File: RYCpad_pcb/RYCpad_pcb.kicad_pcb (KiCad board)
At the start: 2 copper layers, 77.2 x 117.6 mm, 69 parts, among them J1 USB_C_Receptacle_USB2.0, J2 AVR ISP, K1 KEYSW, K10 KEYSW, K11 KEYSW, K12 KEYSW, K13 KEYSW, K14 KEYSW, K15 KEYSW, K16 KEYSW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

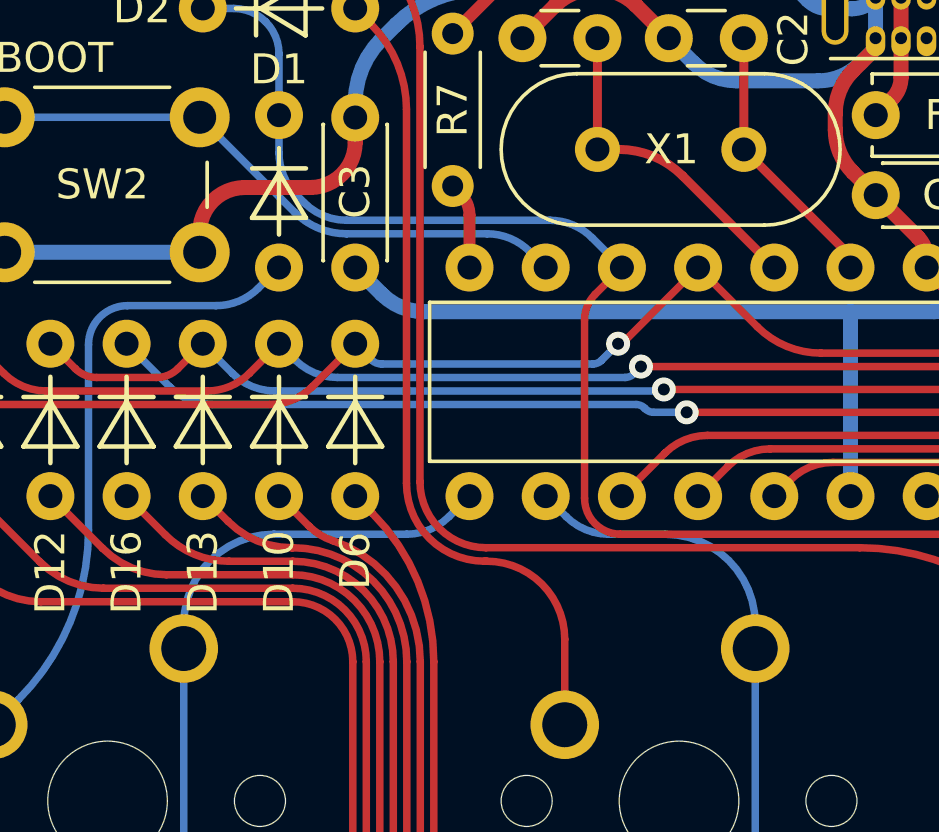
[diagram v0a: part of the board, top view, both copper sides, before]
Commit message: update LED pin
- QMK supports hardware PWM on pin PB1 and PB2 for backlight dimming.
  The hope is that hardware PWM dimming can be exploited for the
  indicator LED, which mitigates any issues related to excessive LED
  brightness.
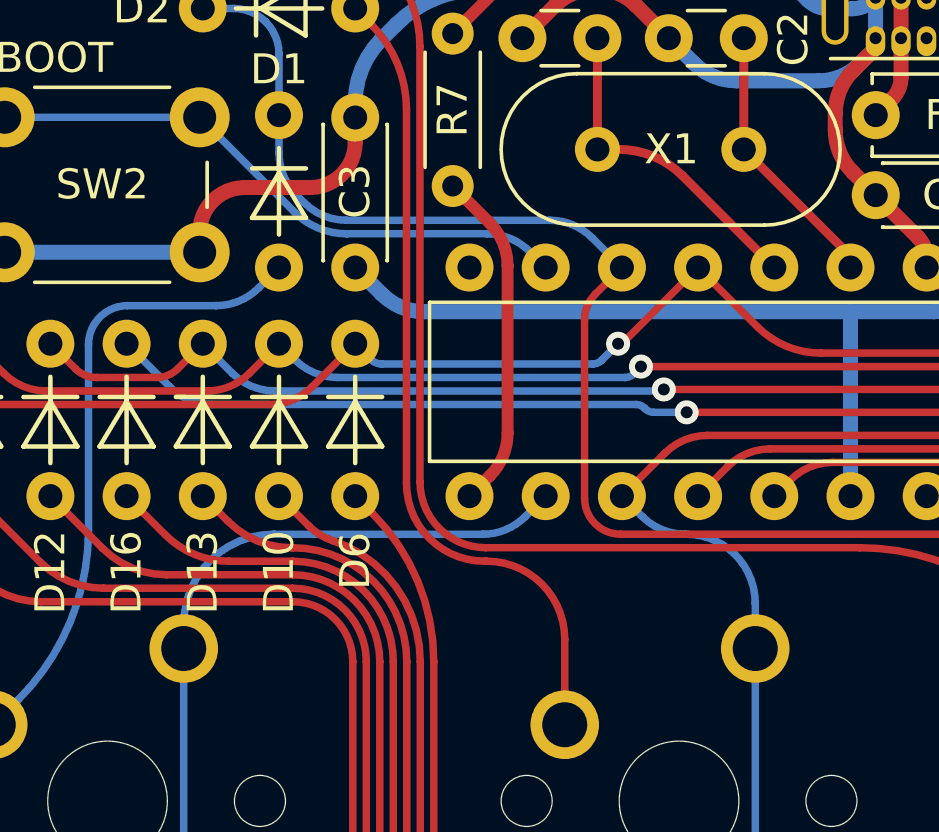
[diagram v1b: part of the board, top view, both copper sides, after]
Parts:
- D20: value LTL-4221N -> LED
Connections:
- J2 pad 4: /MOSI -> /MOSI/col1
- K10 pad 1: /col1 -> /MOSI/col1
- K13 pad 1: /col1 -> /MOSI/col1
- K2 pad 1: /col1 -> /MOSI/col1
- K6 pad 1: /col1 -> /MOSI/col1
- R7 pad 2: Net-(R7-Pad2) -> Net-(U1-Pad15)
- U1 pad 14: Net-(R7-Pad2) -> unconnected-(U1-Pad14)
- U1 pad 15: /col0 -> Net-(U1-Pad15)
- U1 pad 16: /col1 -> /col0
- U1 pad 17: /MOSI -> /MOSI/col1
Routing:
- net /MOSI/col1: track 0.00 -> 112.9 mm
- net /col1: track 67.0 -> 0.00 mm
- net /MOSI: track 48.2 -> 0.00 mm
- net Net-(U1-Pad15): track 0.00 -> 11.4 mm
- net Net-(R7-Pad2): track 2.90 -> 0.00 mm
- net /col0: track 92.1 -> 94.7 mm

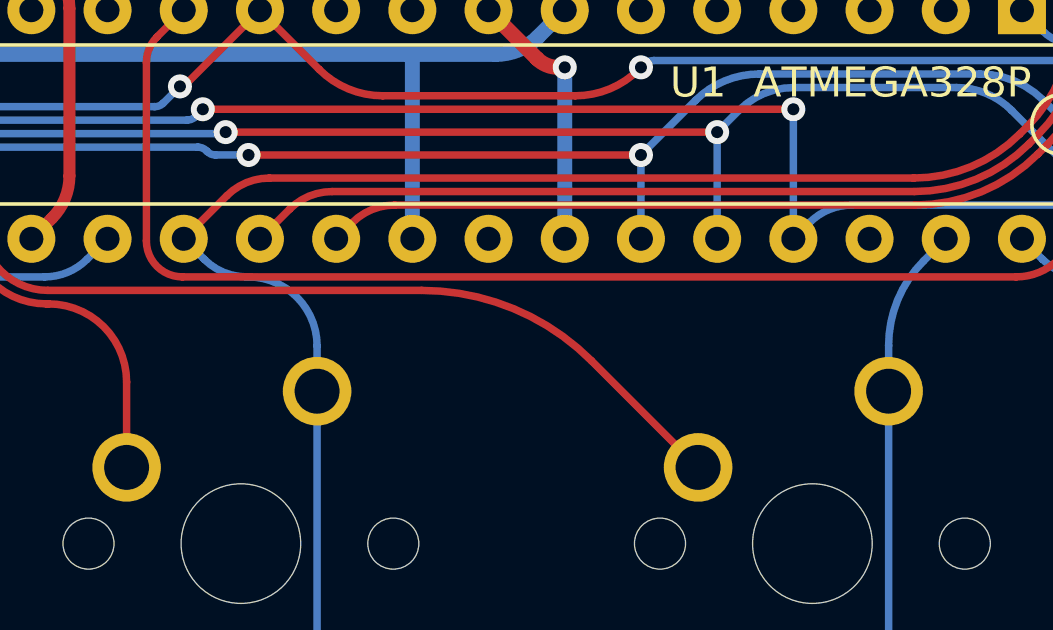
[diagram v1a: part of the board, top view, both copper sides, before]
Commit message: adjust col1 pin
change col1 pin PB3 >>> PC3
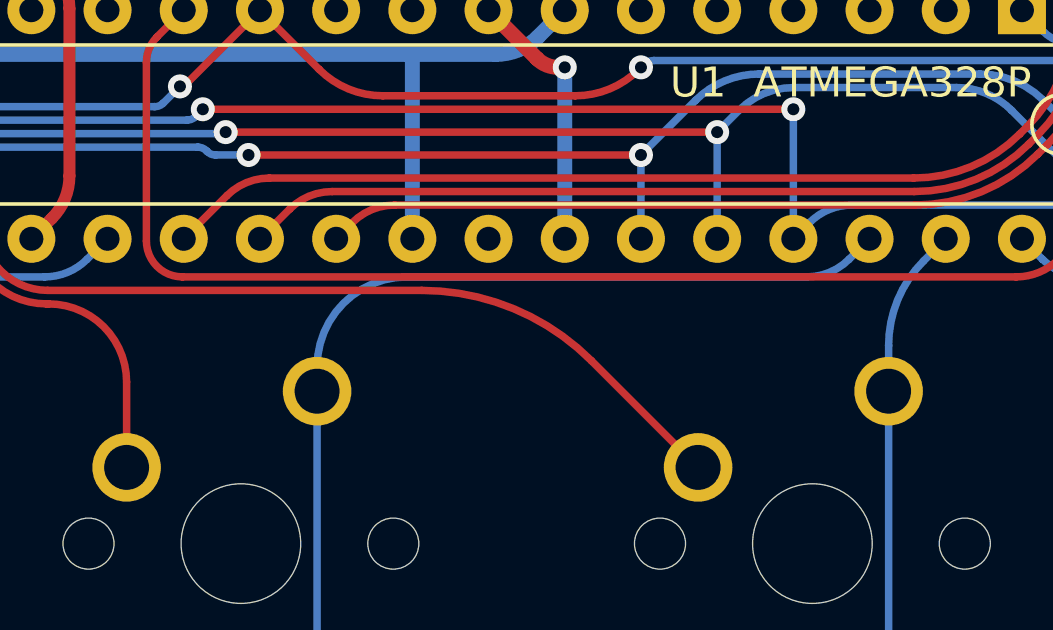
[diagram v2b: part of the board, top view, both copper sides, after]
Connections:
- J2 pad 4: /MOSI/col1 -> /MOSI
- K10 pad 1: /MOSI/col1 -> /col1
- K13 pad 1: /MOSI/col1 -> /col1
- K2 pad 1: /MOSI/col1 -> /col1
- K6 pad 1: /MOSI/col1 -> /col1
- U1 pad 17: /MOSI/col1 -> /MOSI
- U1 pad 26: unconnected-(U1-Pad26) -> /col1
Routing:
- net /MOSI/col1: track 112.9 -> 0.00 mm
- net /col1: track 0.00 -> 78.4 mm
- net /MOSI: track 0.00 -> 48.2 mm
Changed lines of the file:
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@@
   (net 42 "unconnected-(U1-Pad2)")
   (net 43 "Net-(F1-Pad2)")
-  (net 44 "Net-(U1-Pad15)")
+  (net 44 "Net-(R7-Pad2)")
   (net 45 "unconnected-(U1-Pad3)")
   (net 46 "/BOOT")
   (net 47 "unconnected-(U1-Pad6)")
   (net 48 "unconnected-(U1-Pad21)")
-  (net 49 "unconnected-(U1-Pad26)")
-  (net 50 "/MOSI{slash}col1")
-  (net 51 "unconnected-(U1-Pad14)")
+  (net 49 "/MOSI")
+  (net 50 "unconnected-(U1-Pad14)")
+  (net 51 "/col1")
   (footprint "keyswitches:Stabilizer_MX_2u" locked (layer "F.Cu")
     (at 28.575 0 -90)
@@
       (net 46 "/BOOT") (pinfunction "PD7") (pintype "bidirectional"))
     (pad "14" thru_hole oval locked (at 0 33.02 270) (size 1.6 1.6) (drill 0.8) (layers *.Cu *.Mask)
-      (net 51 "unconnected-(U1-Pad14)") (pinfunction "PB0") (pintype "bidirectional+no_connect"))
+      (net 50 "unconnected-(U1-Pad14)") (pinfunction "PB0") (pintype "bidirectional+no_connect"))
     (pad "15" thru_hole oval locked (at 7.62 33.02 270) (size 1.6 1.6) (drill 0.8) (layers *.Cu *.Mask)
-      (net 44 "Net-(U1-Pad15)") (pinfunction "PB1") (pintype "bidirectional"))
+      (net 44 "Net-(R7-Pad2)") (pinfunction "PB1") (pintype "bidirectional"))
     (pad "16" thru_hole oval locked (at 7.62 30.48 270) (size 1.6 1.6) (drill 0.8) (layers *.Cu *.Mask)
       (net 29 "/col0") (pinfunction "PB2") (pintype "bidirectional"))
     (pad "17" thru_hole oval locked (at 7.62 27.94 270) (size 1.6 1.6) (drill 0.8) (layers *.Cu *.Mask)
-      (net 50 "/MOSI{slash}col1") (pinfunction "PB3") (pintype "bidirectional"))
+      (net 49 "/MOSI") (pinfunction "PB3") (pintype "bidirectional"))
     (pad "18" thru_hole oval locked (at 7.62 25.4 270) (size 1.6 1.6) (drill 0.8) (layers *.Cu *.Mask)
       (net 28 "/MISO") (pinfunction "PB4") (pintype "bidirectional"))
@@
       (net 12 "/row2") (pinfunction "PC2") (pintype "bidirectional"))
     (pad "26" thru_hole oval locked (at 7.62 5.08 270) (size 1.6 1.6) (drill 0.8) (layers *.Cu *.Mask)
-      (net 49 "unconnected-(U1-Pad26)") (pinfunction "PC3") (pintype "bidirectional+no_connect"))
+      (net 51 "/col1") (pinfunction "PC3") (pintype "bidirectional"))
     (pad "27" thru_hole oval locked (at 7.62 2.54 270) (size 1.6 1.6) (drill 0.8) (layers *.Cu *.Mask)
       (net 30 "/col2") (pinfunction "PC4") (pintype "bidirectional"))
@@
     (pad "" np_thru_hole circle locked (at 0 0) (size 3.9878 3.9878) (drill 3.9878) (layers *.Cu *.Mask))
     (pad "1" thru_hole circle locked (at 2.54 -5.08) (size 2.286 2.286) (drill 1.4986) (layers *.Cu *.Mask)
-      (net 50 "/MOSI{slash}col1") (pintype "passive"))
+      (net 51 "/col1") (pintype "passive"))
     (pad "2" thru_hole circle locked (at -3.81 -2.54) (size 2.286 2.286) (drill 1.4986) (layers *.Cu *.Mask)
       (net 3 "Net-(D2-Pad2)") (pintype "passive"))
@@
     (pad "" np_thru_hole circle locked (at -5.08 0) (size 1.7018 1.7018) (drill 1.7018) (layers *.Cu *.Mask))
     (pad "1" thru_hole circle locked (at 2.54 -5.08) (size 2.286 2.286) (drill 1.4986) (layers *.Cu *.Mask)
-      (net 50 "/MOSI{slash}col1") (pintype "passive"))
+      (net 51 "/col1") (pintype "passive"))
     (pad "2" thru_hole circle locked (at -3.81 -2.54) (size 2.286 2.286) (drill 1.4986) (layers *.Cu *.Mask)
       (net 8 "Net-(D6-Pad2)") (pintype "passive"))
@@
     (pad "" np_thru_hole circle locked (at 0 0) (size 3.9878 3.9878) (drill 3.9878) (layers *.Cu *.Mask))
     (pad "1" thru_hole circle locked (at 2.54 -5.08) (size 2.286 2.286) (drill 1.4986) (layers *.Cu *.Mask)
-      (net 50 "/MOSI{slash}col1") (pintype "passive"))
+      (net 51 "/col1") (pintype "passive"))
     (pad "2" thru_hole circle locked (at -3.81 -2.54) (size 2.286 2.286) (drill 1.4986) (layers *.Cu *.Mask)
       (net 13 "Net-(D10-Pad2)") (pintype "passive"))
@@
     (pad "" np_thru_hole circle locked (at 0 0) (size 3.9878 3.9878) (drill 3.9878) (layers *.Cu *.Mask))
     (pad "1" thru_hole circle locked (at 2.54 -5.08) (size 2.286 2.286) (drill 1.4986) (layers *.Cu *.Mask)
-      (net 50 "/MOSI{slash}col1") (pintype "passive"))
+      (net 51 "/col1") (pintype "passive"))
     (pad "2" thru_hole circle locked (at -3.81 -2.54) (size 2.286 2.286) (drill 1.4986) (layers *.Cu *.Mask)
       (net 17 "Net-(D13-Pad2)") (pintype "passive"))
@@
       (net 26 "/SCK") (pinfunction "Pin_3") (pintype "passive"))
     (pad "4" thru_hole oval locked (at 2.54 2.54 90) (size 1.7 1.7) (drill 1) (layers *.Cu *.Mask)
-      (net 50 "/MOSI{slash}col1") (pinfunction "Pin_4") (pintype "passive"))
+      (net 49 "/MOSI") (pinfunction "Pin_4") (pintype "passive"))
     (pad "5" thru_hole oval locked (at 0 5.08 90) (size 1.7 1.7) (drill 1) (layers *.Cu *.Mask)
       (net 25 "/RESET") (pinfunction "Pin_5") (pintype "passive"))
@@
       (net 41 "Net-(D20-Pad2)") (pintype "passive"))
     (pad "2" thru_hole oval locked (at 5.08 0 270) (size 1.4 1.4) (drill 0.7) (layers *.Cu *.Mask)
-      (net 44 "Net-(U1-Pad15)") (pintype "passive"))
+      (net 44 "Net-(R7-Pad2)") (pintype "passive"))
     (model "${KISYS3DMOD}/Resistor_THT.3dshapes/R_Axial_DIN0204_L3.6mm_D1.6mm_P5.08mm_Horizontal.wrl"
       (offset (xyz 0 0 0))
@@
   (arc (start -22.33859 -48.19759) (mid -21.543753 -47.666496) (end -20.606178 -47.480001) (width 0.25) (layer "B.Cu") (net 46))
   (arc (start -14.509214 -46.894214) (mid -15.158061 -47.32776) (end -15.923428 -47.480001) (width 0.25) (layer "B.Cu") (net 46))
-  (segment (start 19.661 -56.388) (end 20.888573 -56.388) (width 0.25) (layer "F.Cu") (net 50))
-  (segment (start -8.576552 -40.760021) (end 12.897903 -40.760021) (width 0.25) (layer "F.Cu") (net 50))
-  (segment (start 22.302787 -56.973787) (end 22.987 -57.658) (width 0.25) (layer "F.Cu") (net 50))
-  (segment (start -11.43 -38.735) (end -9.990765 -40.174235) (width 0.25) (layer "F.Cu") (net 50))
-  (segment (start 18.161 -46.023118) (end 18.161 -54.888) (width 0.25) (layer "F.Cu") (net 50))
-  (segment (start 16.433437 -42.224487) (end 16.696534 -42.487584) (width 0.25) (layer "F.Cu") (net 50))
-  (arc (start -9.990765 -40.174235) (mid -9.341919 -40.60778) (end -8.576552 -40.760021) (width 0.25) (layer "F.Cu") (net 50))
-  (arc (start 19.661 -56.388) (mid 18.60034 -55.94866) (end 18.161 -54.888) (width 0.25) (layer "F.Cu") (net 50))
-  (arc (start 18.161 -46.023118) (mid 17.780398 -44.109701) (end 16.696534 -42.487584) (width 0.25) (layer "F.Cu") (net 50))
-  (arc (start 20.888573 -56.388) (mid 21.65394 -56.540241) (end 22.302787 -56.973787) (width 0.25) (layer "F.Cu") (net 50))
-  (arc (start 16.433437 -42.224487) (mid 14.81132 -41.140623) (end 12.897903 -40.760021) (width 0.25) (layer "F.Cu") (net 50))
-  (segment (start -6.985 -35.165) (end -6.985 -33.655) (width 0.25) (layer "B.Cu") (net 50))
-  (segment (start -6.985 -33.655) (end -6.985 -14.605) (width 0.25) (layer "B.Cu") (net 50))
-  (segment (start -6.985 -10.324666) (end -6.985 4.445) (width 0.25) (layer "B.Cu") (net 50))
-  (segment (start -6.985 4.445) (end -6.985 23.495) (width 0.25) (layer "B.Cu") (net 50))
-  (segment (start -6.985 -14.605) (end -6.985 -10.324666) (width 0.25) (layer "B.Cu") (net 50))
-  (segment (start -9.331573 -37.465) (end -9.285 -37.465) (width 0.25) (layer "B.Cu") (net 50))
-  (segment (start -11.43 -38.735) (end -10.745786 -38.050786) (width 0.25) (layer "B.Cu") (net 50))
-  (arc (start -9.331573 -37.465) (mid -10.09694 -37.617241) (end -10.745786 -38.050786) (width 0.25) (layer "B.Cu") (net 50))
-  (arc (start -9.285 -37.465) (mid -7.658654 -36.791346) (end -6.985 -35.165) (width 0.25) (layer "B.Cu") (net 50))
+  (segment (start 19.661 -56.388) (end 20.888573 -56.388) (width 0.25) (layer "F.Cu") (net 49))
+  (segment (start -8.576552 -40.760021) (end 12.897903 -40.760021) (width 0.25) (layer "F.Cu") (net 49))
+  (segment (start 22.302787 -56.973787) (end 22.987 -57.658) (width 0.25) (layer "F.Cu") (net 49))
+  (segment (start -11.43 -38.735) (end -9.990765 -40.174235) (width 0.25) (layer "F.Cu") (net 49))
+  (segment (start 18.161 -46.023118) (end 18.161 -54.888) (width 0.25) (layer "F.Cu") (net 49))
+  (segment (start 16.433437 -42.224487) (end 16.696534 -42.487584) (width 0.25) (layer "F.Cu") (net 49))
+  (arc (start -9.990765 -40.174235) (mid -9.341919 -40.60778) (end -8.576552 -40.760021) (width 0.25) (layer "F.Cu") (net 49))
+  (arc (start 19.661 -56.388) (mid 18.60034 -55.94866) (end 18.161 -54.888) (width 0.25) (layer "F.Cu") (net 49))
+  (arc (start 18.161 -46.023118) (mid 17.780398 -44.109701) (end 16.696534 -42.487584) (width 0.25) (layer "F.Cu") (net 49))
+  (arc (start 20.888573 -56.388) (mid 21.65394 -56.540241) (end 22.302787 -56.973787) (width 0.25) (layer "F.Cu") (net 49))
+  (arc (start 16.433437 -42.224487) (mid 14.81132 -41.140623) (end 12.897903 -40.760021) (width 0.25) (layer "F.Cu") (net 49))
+  (segment (start -6.985 -33.655) (end -6.985 -14.605) (width 0.25) (layer "B.Cu") (net 51))
+  (segment (start -6.985 -10.324666) (end -6.985 4.445) (width 0.25) (layer "B.Cu") (net 51))
+  (segment (start -6.985 4.445) (end -6.985 23.495) (width 0.25) (layer "B.Cu") (net 51))
+  (segment (start 9.331573 -37.465) (end -3.985 -37.465) (width 0.25) (layer "B.Cu") (net 51))
+  (segment (start 11.43 -38.735) (end 10.745786 -38.050786) (width 0.25) (layer "B.Cu") (net 51))
+  (segment (start -6.985 -14.605) (end -6.985 -10.324666) (width 0.25) (layer "B.Cu") (net 51))
+  (segment (start -6.985 -34.465) (end -6.985 -33.655) (width 0.25) (layer "B.Cu") (net 51))
+  (arc (start -3.985 -37.465) (mid -6.10632 -36.58632) (end -6.985 -34.465) (width 0.25) (layer "B.Cu") (net 51))
+  (arc (start 10.745786 -38.050786) (mid 10.09694 -37.617241) (end 9.331573 -37.465) (width 0.25) (layer "B.Cu") (net 51))
   (group "" (id 778130e2-5dcf-4ba4-bd77-4acc3a461105)
     (members

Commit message: change LED resistor default value
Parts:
- R7: value 1k -> 330
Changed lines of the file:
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@@
       (effects (font (size 1 1) (thickness 0.15)))
     )
-    (fp_text value "1k" (at 2.54 1.92 90) (layer "F.Fab")
+    (fp_text value "330" (at 2.54 1.92 90) (layer "F.Fab")
       (effects (font (size 1 1) (thickness 0.15)))
     )
